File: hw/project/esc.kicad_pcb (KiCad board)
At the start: 4 copper layers, 125 x 80 mm, 185 parts, among them J1 KFA-1016-10_16-2P, J10 I2C, J11 Misc, J12 Voltage Monitor, J2 KFA-1016-10_16-3P, J3 FTSH-107-01-L-DV-K-A, J4 Throttle, J5 Hall, J6 Serial, J7 2.54 Comm, J8 SPI, J9 CAN, Q1 SUM110P06-08L-E3, Q2 SUM110P06-08L-E3, Q3 STL110N10F7, Q4 STL110N10F7, Q5 STL110N10F7, Q6 STL110N10F7, Q7 STL110N10F7, Q8 STL110N10F7, SW1 BOOT0, SW2 RESET, SW3 USER, U1 STSPIN32G4, U2 LMR51610XDBVR, U3 ATA6561-GAQW-N, X1 SWXC5ACVF0-32.000000

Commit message: Place back copper pours and thermal vias throughout power section
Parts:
- moved C35 1.47 mm to (80.3, 54.4), turned to 180 degrees
- moved C37 1.46 mm to (80.3, 88.9), turned to 180 degrees
- moved C36 1.42 mm to (80.3, 71.6), turned to 180 degrees
- moved R35 1.05 mm to (80.3, 69.9), turned to 0 degrees
- moved R34 1.04 mm to (80.3, 52.6), turned to 0 degrees
- moved R36 1.04 mm to (80.3, 87.1), turned to 0 degrees
- moved TP10 0.25 mm to (108.2, 36.3)
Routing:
- net VM: track 0.00 -> 0.18 mm, vias 0 -> 103
- net /Peripherals/VM_IN: track 0.00 -> 0.12 mm, vias 0 -> 28
- net PGND: vias 0 -> 60
- net /Drive/W: vias 0 -> 54
- net /Drive/VSHUNT_W+: vias 0 -> 7
- net /Drive/VSHUNT_V+: vias 0 -> 7
- net /Drive/VSHUNT_U+: vias 0 -> 7
- net /Drive/V: vias 0 -> 54
- net /Drive/U: vias 0 -> 54
- added copper zone on B.Cu, net /Drive/U
- added copper zone on B.Cu, net /Drive/V
- added copper zone on B.Cu, net /Drive/VSHUNT_U+
- added copper zone on F.Cu, net /Drive/VSHUNT_U+
- added copper zone on B.Cu, net /Drive/VSHUNT_V+
- added copper zone on F.Cu, net /Drive/VSHUNT_V+
- added copper zone on B.Cu, net /Drive/VSHUNT_W+
- added copper zone on F.Cu, net /Drive/VSHUNT_W+
- added copper zone on B.Cu, net /Drive/W
- added copper zone on B.Cu, net /Peripherals/VM_IN
- added copper zone on B.Cu, net Net-(D3-K)
- added copper zone on B.Cu, net PGND
- added copper zone on B.Cu, net VM

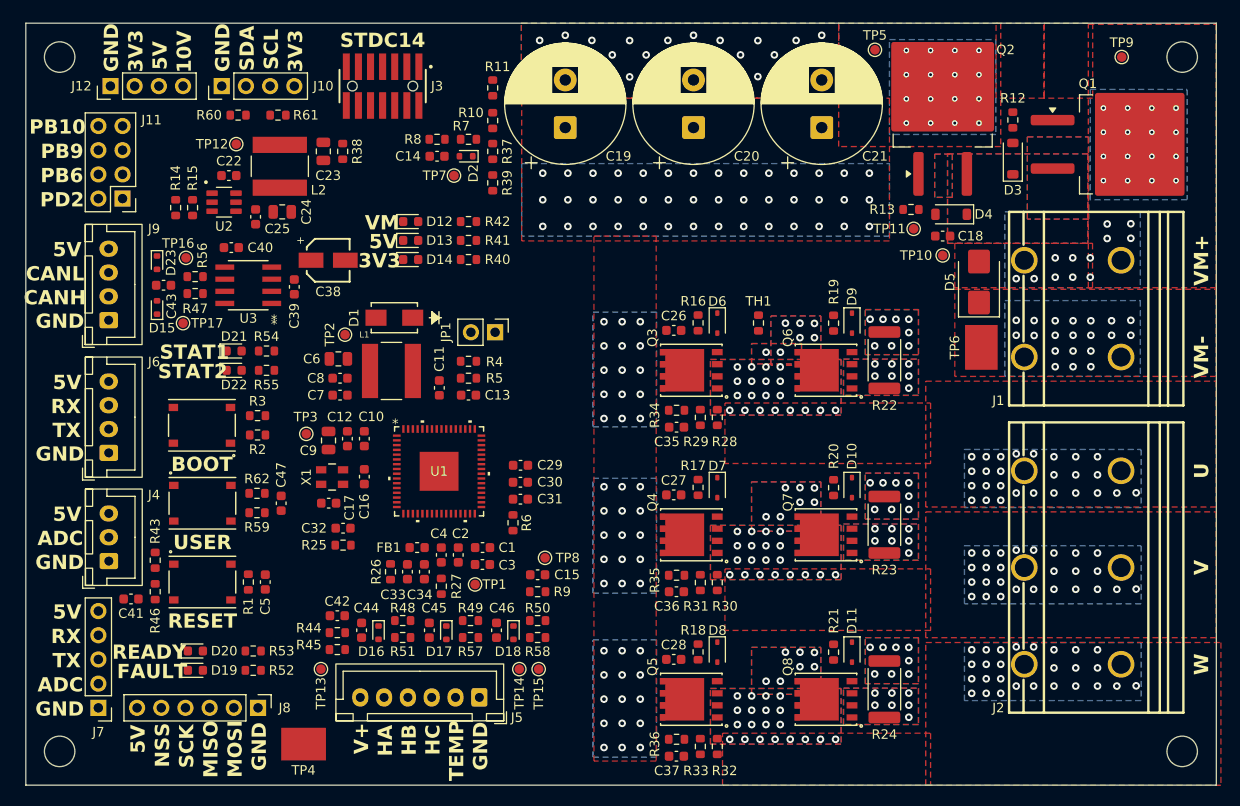
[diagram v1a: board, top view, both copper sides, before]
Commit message: Resolve silkscreen and solder mask expansion errors before routing
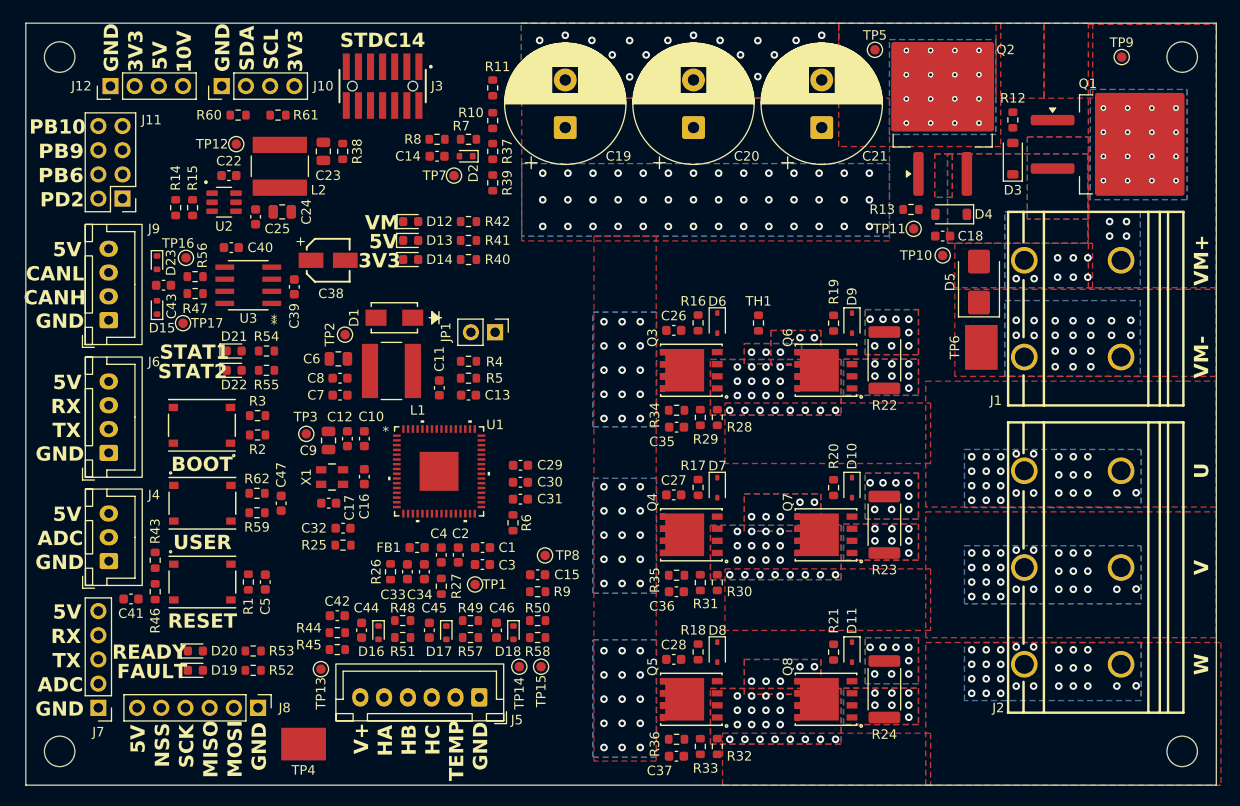
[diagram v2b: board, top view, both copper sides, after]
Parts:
- J1: value KFA-1016-10_16-2P -> ~
- J2: value KFA-1016-10_16-3P -> ~
- TP1, TP10, TP11, TP12, TP13, TP14, TP15, TP16, TP17, TP2, TP3, TP5, TP7, TP8, TP9: footprint TestPoint:TestPoint_Pad_D1.0mm -> esc:TestPoint_Pad_D1.0mm_with_More_Clearance
- moved TP15 0.36 mm to (66.0, 79.5)
- moved TP14 0.25 mm to (63.8, 79.5)
- moved TP8 0.25 mm to (66.5, 67.8)
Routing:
- net /Drive/W: vias 54 -> 52
- net /Drive/V: vias 54 -> 52
- net /Drive/U: vias 54 -> 52

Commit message: Add colours to named nets
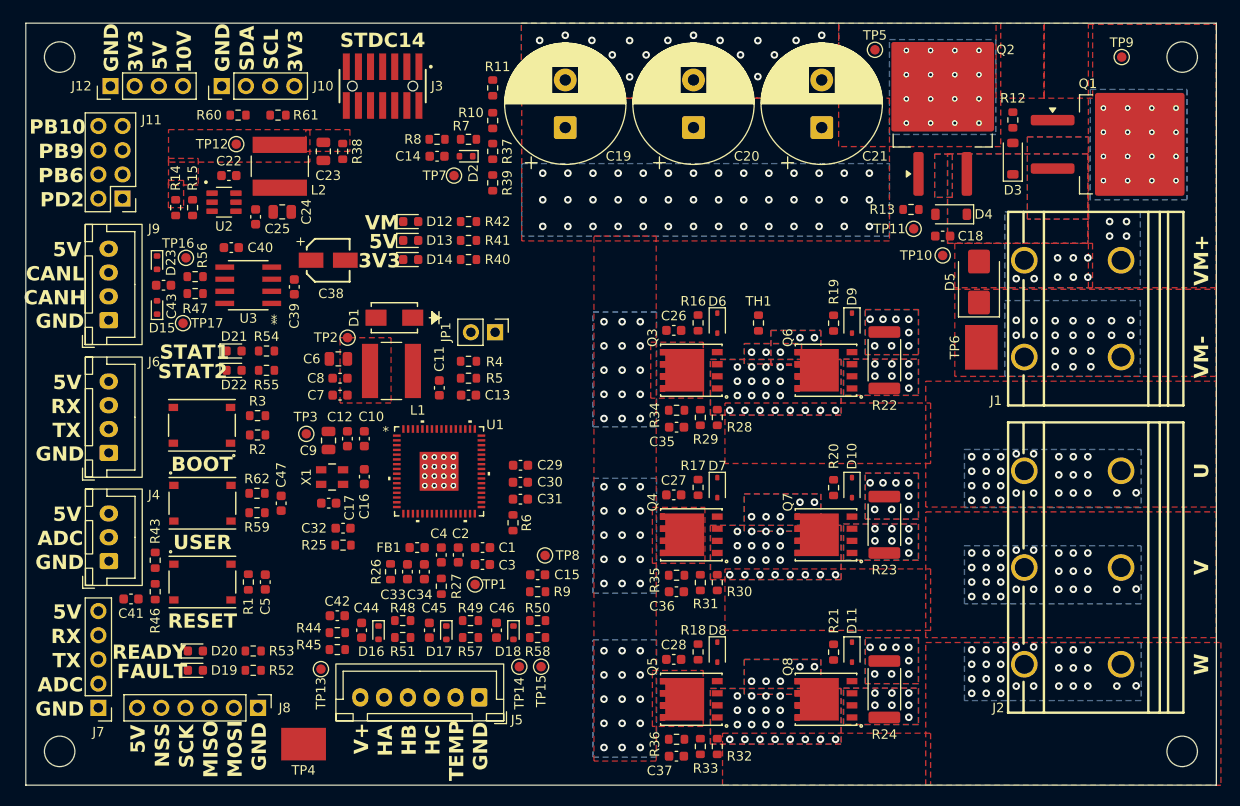
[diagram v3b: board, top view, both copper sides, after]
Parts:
- moved TP2 0.41 mm to (45.7, 45.0)
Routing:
- net GND: vias 0 -> 16
- added copper zone on F.Cu, net 5V
- added copper zone on F.Cu, net VCC

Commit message: Place all vias
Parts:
- C38: footprint WCAP-ASLI_4X5.5:WCAP-ASLI_4X5.5_DXL_ -> EEEFKC220UAR:EEEFKC220UAR
- J1: value ~ -> KFA-1016-10_16-2P
- J2: value ~ -> KFA-1016-10_16-3P
- L1: footprint IND_ASPI-6045S-180M-T:IND_ASPI-6045S-180M-T -> Inductor_SMD:L_Sunlord_SWPA6045S
- L2: footprint IND_ASPI-6045S-330M-T:IND_ASPI-6045S-330M-T -> Inductor_SMD:L_Sunlord_SWPA6045S
- moved R26 1.78 mm to (52.0, 69.5)
- moved C33 1.72 mm to (50.3, 69.5)
- moved C34 1.53 mm to (53.8, 71.1)
- moved D14 1.02 mm to (52.3, 37.8)
- moved R40 1.02 mm to (58.4, 37.8)
- moved TP1 0.64 mm to (59.7, 71.1)
- moved D13 0.51 mm to (52.3, 35.3)
- moved R41 0.51 mm to (58.4, 35.3)
- moved C32 0.32 mm to (45.2, 65.3)
- moved R25 0.32 mm to (45.2, 67.1)
- moved TP2 0.25 mm to (45.7, 44.7)
- turned C38 to 0 degrees
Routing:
- net PGND: vias 60 -> 96
- net GND: vias 16 -> 124
- added copper zone on F.Cu, net VDD

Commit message: Trace GHSx, GLSx, BOOTx
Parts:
- moved C29 0.45 mm to (63.9, 57.9)
- moved C30 0.19 mm to (63.9, 59.9)
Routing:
- net /Control/GLS3: track 0.00 -> 52.4 mm, vias 0 -> 2
- net /Control/GLS1: track 0.00 -> 50.8 mm, vias 0 -> 2
- net /Control/GLS2: track 0.00 -> 43.9 mm, vias 0 -> 2
- net /Drive/W: track 0.00 -> 40.2 mm, vias 52 -> 53
- net /Control/GHS3: track 0.00 -> 35.4 mm, vias 0 -> 2
- net /Control/GHS1: track 0.00 -> 34.3 mm, vias 0 -> 2
- net /Drive/U: track 0.00 -> 30.5 mm, vias 52 -> 53
- net /Drive/V: track 0.00 -> 29.7 mm, vias 52 -> 53
- net /Control/GHS2: track 0.00 -> 25.8 mm, vias 0 -> 2
- net Net-(D6-A): track 0.00 -> 4.12 mm
- net Net-(D7-A): track 0.00 -> 4.12 mm
- net Net-(D8-A): track 0.00 -> 4.12 mm
- net Net-(D11-A): track 0.00 -> 4.02 mm
- net Net-(D9-A): track 0.00 -> 4.02 mm
- net Net-(D10-A): track 0.00 -> 4.02 mm
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
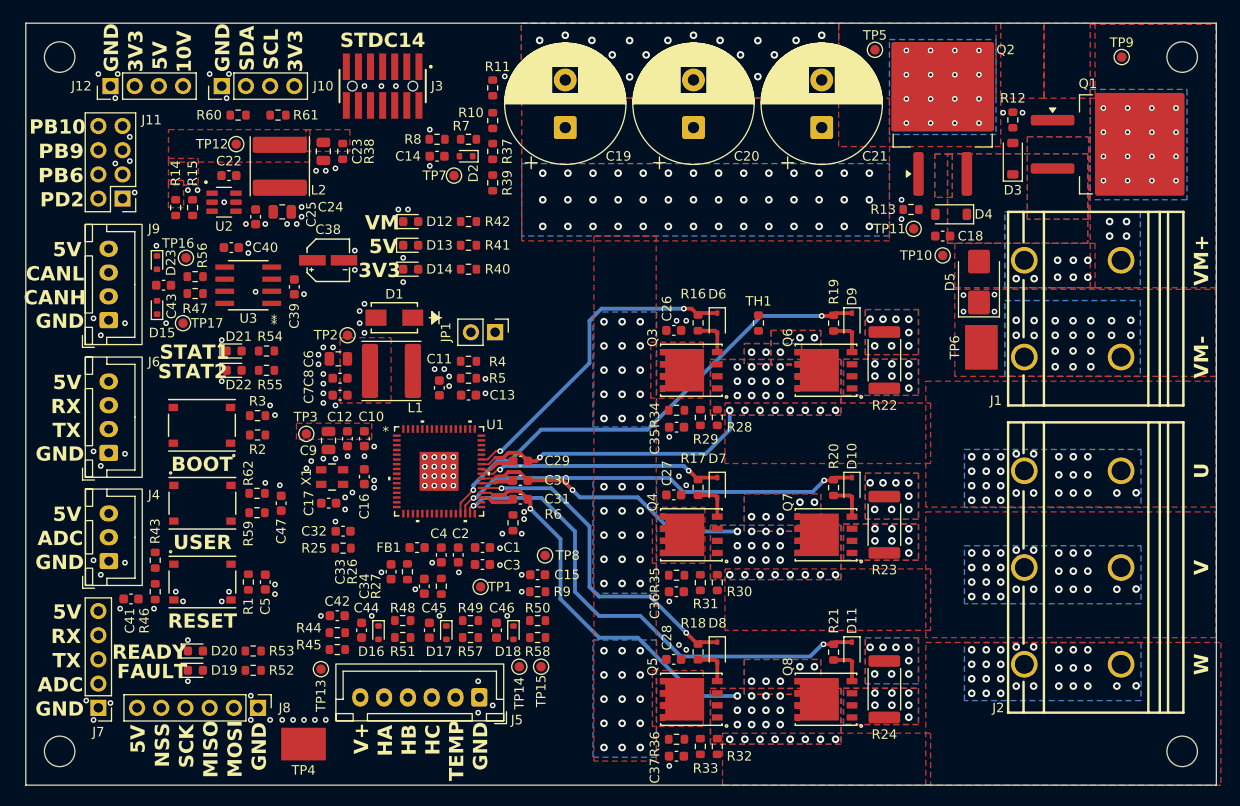
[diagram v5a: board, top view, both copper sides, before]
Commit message: Route traces internal to power sections
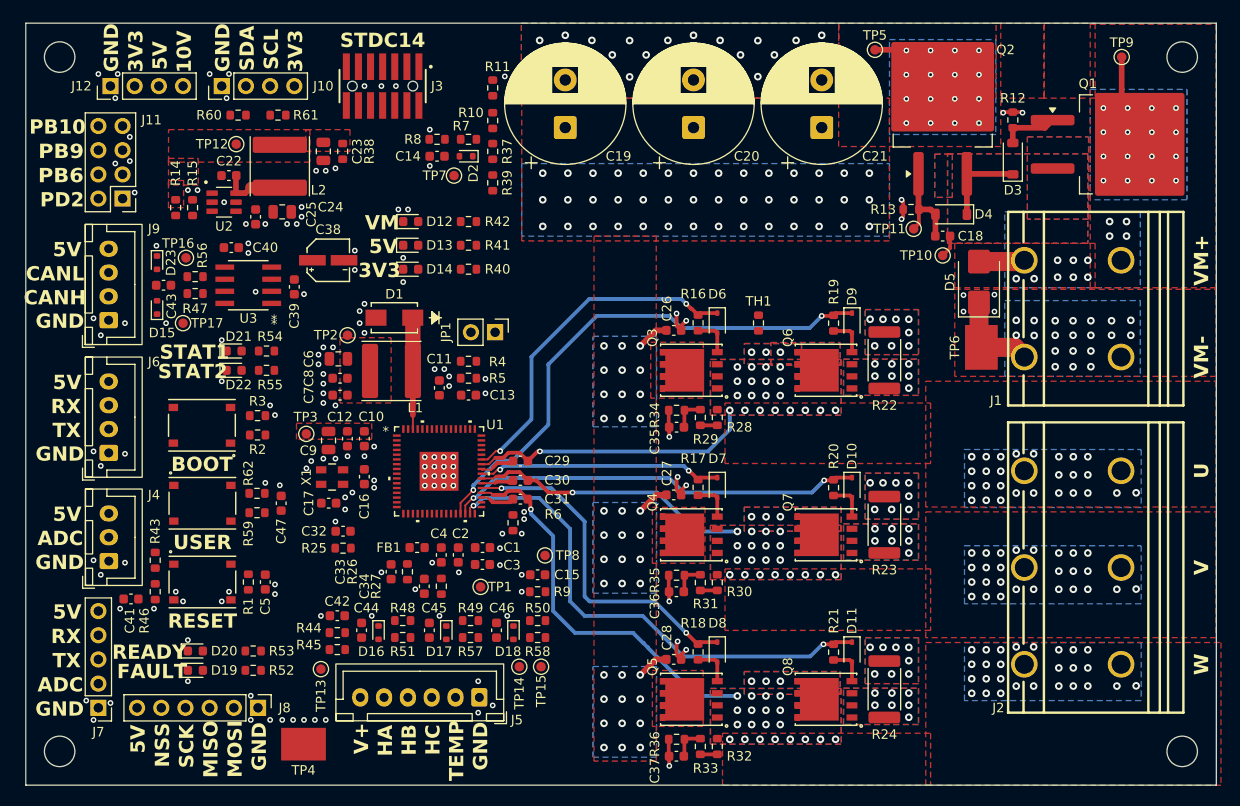
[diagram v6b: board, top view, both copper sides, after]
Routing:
- net PGND: track 0.01 -> 23.9 mm
- net VM: track 0.18 -> 19.2 mm, vias 103 -> 94
- net /Peripherals/VM_IN: track 0.12 -> 14.9 mm
- net /Control/SW: track 0.00 -> 11.7 mm
- net Net-(D3-K): track 0.00 -> 11.4 mm
- net Net-(D4-A): track 0.00 -> 10.2 mm
- net GND: track 0.00 -> 8.41 mm
- net Net-(U2-SW): track 0.00 -> 6.69 mm
- net Net-(D3-A): track 0.00 -> 6.10 mm
- net /Control/GLS1: track 50.8 -> 55.5 mm
- net /Control/VPHASE_W: track 0.00 -> 3.51 mm
- net /Control/VPHASE_U: track 0.00 -> 3.50 mm
- net /Control/VPHASE_V: track 0.00 -> 3.45 mm
- net /Control/GHS1: track 34.3 -> 36.4 mm
- net Net-(R32-Pad2): track 0.00 -> 1.78 mm
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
